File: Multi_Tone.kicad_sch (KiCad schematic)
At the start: 0 parts

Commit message: Added band-pass filter, ac-dc power, low-pass filter
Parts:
- added BR1: DB107-BP, symbol Device:D_Bridge_+-AA
- added C1, C3: 100u, symbol Device:C_Polarized
- added C2, C9: 470u, symbol Device:C_Polarized
- added C4, C5: 100n, symbol Device:C
- added C6: 10n, symbol Device:C
- added C7: 33n, symbol Device:C
- added D1: LED Y, symbol Device:LED
- added D2, D5: 1N4148, Diode_THT:D_DO-35_SOD27_P7.62mm_Horizontal, symbol Diode:1N4148
- added D3: LEDR, symbol Device:LED
- added D4: LEDG, symbol Device:LED
- added DR: R16, symbol Device:R
- added J1: PW_OUTPUT, symbol Connector_Generic:Conn_01x03
- added J2: PW_INPUT, symbol Connector_Generic:Conn_01x03
- added Q1, Q2: 2N3904, Package_TO_SOT_THT:TO-92_Inline, symbol Transistor_BJT:2N3904
- added R1: 1k, symbol Device:R
- added R10: 36k, symbol Device:R
- added R2, R6: 16K, symbol Device:R
- added R3, R4: 470R, symbol Device:R
- added R5, R7, R8: 4k7, symbol Device:R
- added R9: 47k, symbol Device:R
- added TP1, TP10, TP2, TP3, TP4, TP5, TP6, TP7, TP8, TP9: TestPoint, symbol Connector:TestPoint
- added U1: L7812, symbol Regulator_Linear:L7812
- added U2: L7912, symbol Regulator_Linear:L7912
- added U3, U4: LM2902, symbol Amplifier_Operational:LM2902
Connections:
- new net: D2.1 (K), R5.1
- new net: Q1.2 (B), R5.2, TP8.1
- new net: D3.2 (A), R4.2
- new net: BR1.1 (+), C9.1, U1.1 (IN)
- new net: BR1.2 (-), C2.2, U2.2 (VI)
- new net: C4.2, R2.2, R6.1
- new net: C6.1, C7.1, R10.1, R9.2
- new net: D5.1 (K), R7.1
- new net: Q2.2 (B), R7.2, TP9.1
- new net: D4.1 (K), Q2.3 (C)
- new net: D1.2 (A), R1.1
- new net: U3.13 (-), U3.14
- new net: D4.2 (A), R3.2
- new net: D3.1 (K), Q1.3 (C)
- new net: C7.2, R8.1, U3.6 (-)
- new net: C5.1, R6.2, U4.3 (+)
- new net +12V: C1.1, J1.3 (Pin_3), R3.1, R4.1, TP4.1, U1.3 (OUT)
- new net -12V: C3.2, D1.1 (K), J1.1 (Pin_1), TP5.1, U2.3 (VO)
- new net GND: C1.2, C3.1, C5.2, DR.2, J1.2 (Pin_2), Q1.1 (E), Q2.1 (E), R1.2, R9.1, TP3.1, TP6.1, U1.2 (GND), U2.1 (GND), U3.12 (+), U3.5 (+)
- new net GNDPWR: C2.1, C9.2, DR.1, J2.2 (Pin_2)
- new net OUT_LOW: C4.1, D2.2 (A), TP7.1, U4.1, U4.2 (-)
- new net OUT_MID: C6.2, D5.2 (A), R8.2, TP10.1, U3.7
- new net VAC+: BR1.3, J2.1 (Pin_1), TP1.1
- new net VAC-: BR1.4, J2.3 (Pin_3), TP2.1
- new net V_AMP: R10.2, R2.1
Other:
- note added: "AC TO DC +/-12V"
- note added: "LOW PASS FILTER"
- note added: "NEAR POWER INPUT"

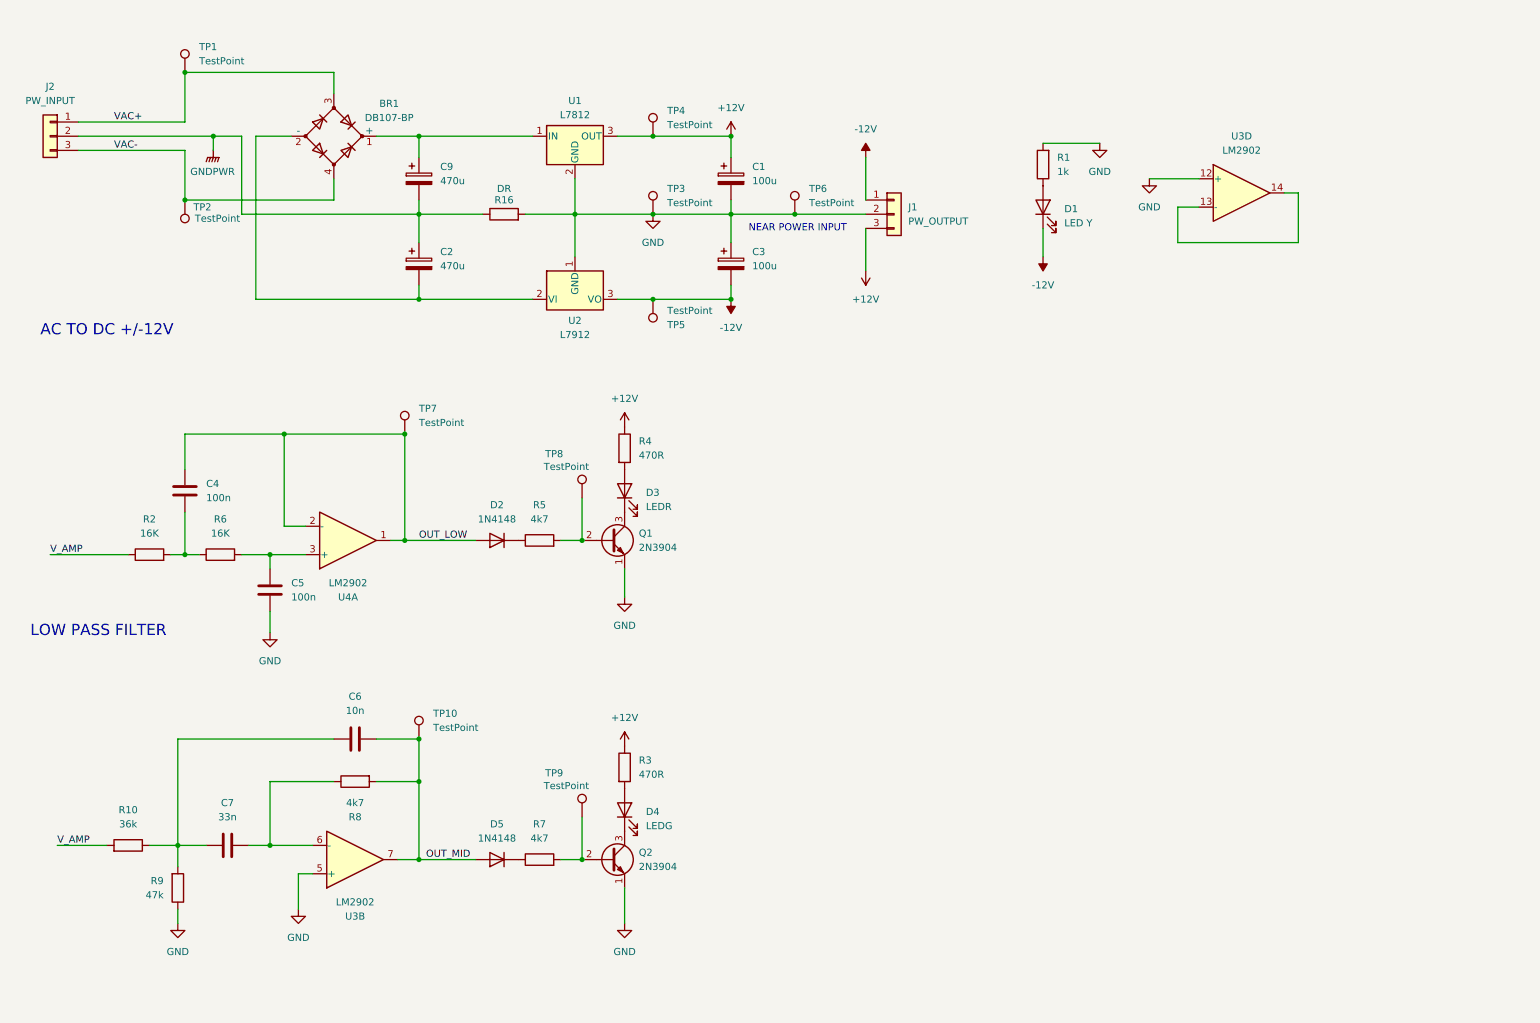
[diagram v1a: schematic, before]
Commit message: Completed schematic layout of music visualiser circuit.
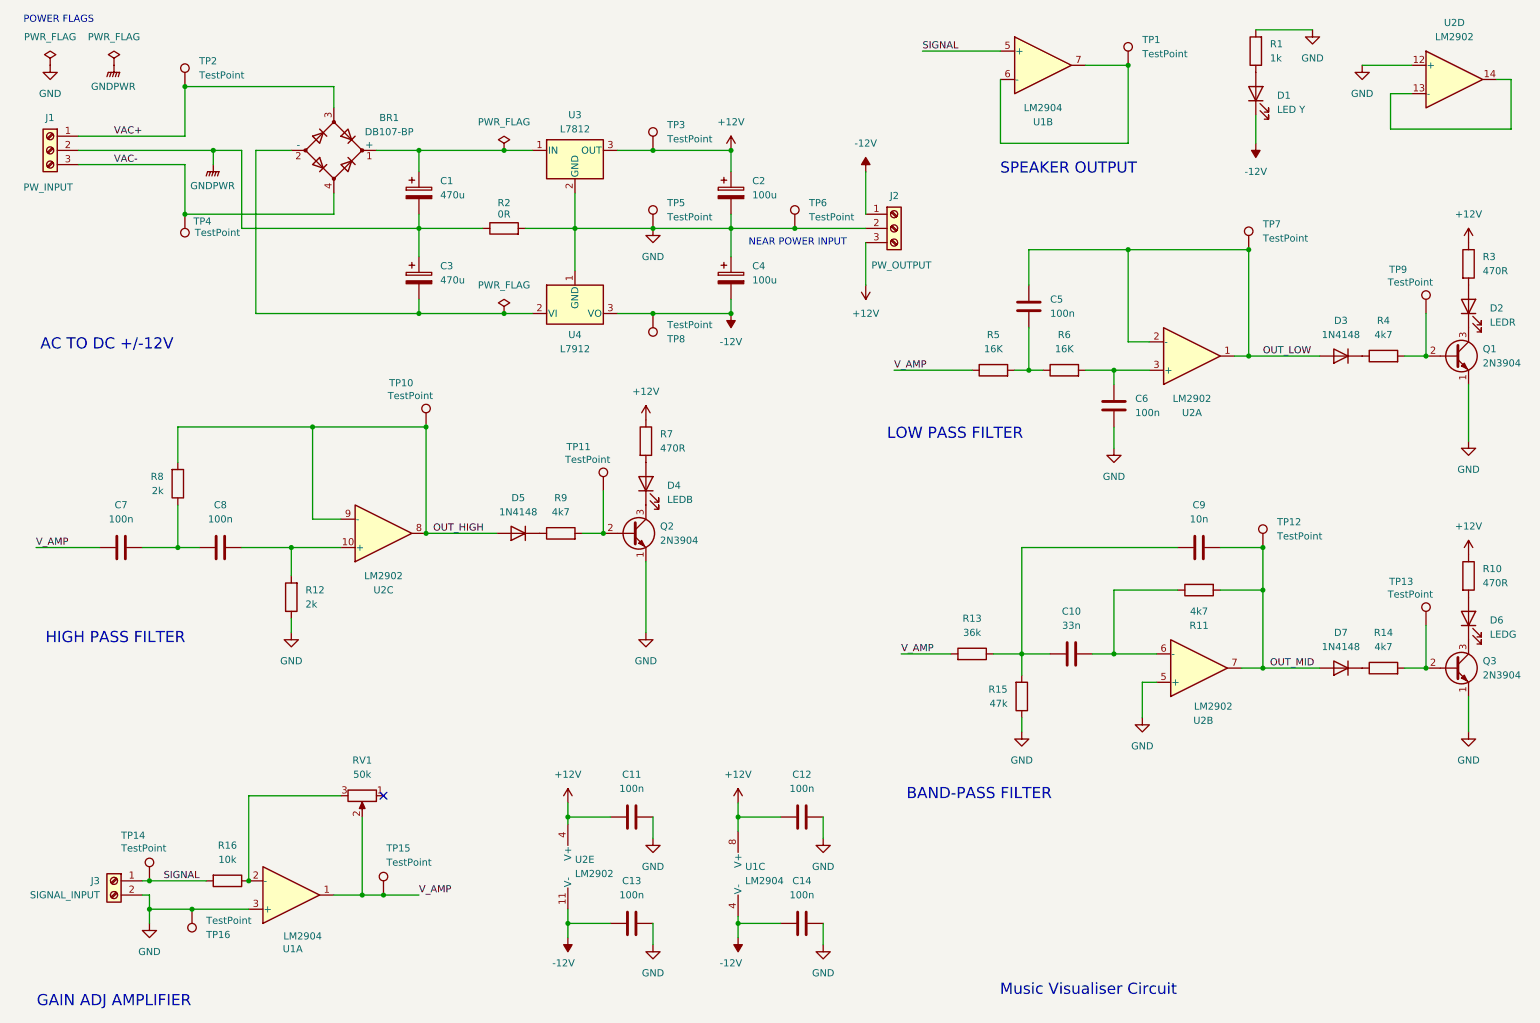
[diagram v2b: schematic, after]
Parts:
- removed J1: PW_OUTPUT, symbol Connector_Generic:Conn_01x03
- removed J2: PW_INPUT, symbol Connector_Generic:Conn_01x03
- added C11, C12, C13, C14, C7, C8: 100n, symbol Device:C
- added D4: LEDB, symbol Device:LED
- added D5: 1N4148, Diode_THT:D_DO-35_SOD27_P7.62mm_Horizontal, symbol Diode:1N4148
- added J1: PW_INPUT, symbol Connector:Screw_Terminal_01x03
- added J2: PW_OUTPUT, symbol Connector:Screw_Terminal_01x03
- added J3: SIGNAL_INPUT, symbol Connector:Screw_Terminal_01x02
- added Q2: 2N3904, Package_TO_SOT_THT:TO-92_Inline, symbol Transistor_BJT:2N3904
- added R12, R8: 2k, symbol Device:R
- added R16: 10k, symbol Device:R
- added R7: 470R, symbol Device:R
- added R9: 4k7, symbol Device:R
- added RV1: 50k, symbol Device:R_Potentiometer
- added TP1, TP10, TP11, TP14, TP15, TP16: TestPoint, symbol Connector:TestPoint
- added U1: LM2904, symbol Amplifier_Operational:LM2904
- added unit 5 of U2
- added unit 3 of U2
- R2: renamed from DR; value R16 -> 0R
- renumbered C9 to C1, C7 to C10, C1 to C2, C2 to C3, C3 to C4, C4 to C5, C5 to C6, C6 to C9, D3 to D2, D2 to D3, D4 to D6, D5 to D7, Q2 to Q3, R3 to R10, R8 to R11, R10 to R13, R7 to R14, R9 to R15, R4 to R3, R5 to R4, R2 to R5, TP10 to TP12, TP9 to TP13, TP1 to TP2, TP4 to TP3, TP2 to TP4, TP3 to TP5, TP5 to TP8, TP8 to TP9, U3 to U2, U4 to U2, U1 to U3, U2 to U4
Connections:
- net +12V: now also C11.1, C12.1, J2.3 (Pin_3), R7.1, U1.8 (V+), U2.4 (V+)
- net -12V: now also C13.2, C14.2, J2.1 (Pin_1), U1.4 (V-), U2.11 (V-)
- net GND: now also C11.2, C12.2, C13.1, C14.1, J2.2 (Pin_2), J3.2 (Pin_2), Q2.1 (E), R12.1, TP16.1, U1.3 (+)
- net GNDPWR: now also J1.2 (Pin_2)
- net VAC+: now also J1.1 (Pin_1)
- net VAC-: now also J1.3 (Pin_3)
- net V_AMP: now also C7.1, RV1.2, TP15.1, U1.1
- new net: C7.2, C8.1, R8.1
- new net: D5.1 (K), R9.1
- new net: C8.2, R12.2, U2.10 (+)
- new net: Q2.2 (B), R9.2, TP11.1
- new net: D4.1 (K), Q2.3 (C)
- new net: R16.1, RV1.3, U1.2 (-)
- new net: D4.2 (A), R7.2
- new net: TP1.1, U1.6 (-), U1.7
- new net OUT_HIGH: D5.2 (A), R8.2, TP10.1, U2.8, U2.9 (-)
- new net SIGNAL: J3.1 (Pin_1), R16.2, TP14.1, U1.5 (+)
- no-connect marks 0 -> 1
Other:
- note added: "BAND-PASS FILTER"
- note added: "GAIN ADJ AMPLIFIER"
- note added: "HIGH PASS FILTER"
- note added: "Music Visualiser Circuit"
- note added: "POWER FLAGS"
- note added: "SPEAKER OUTPUT"
- moved on the sheet: BR1, C1, C10, C2, C3, C4, C5, C6, C9, D1, D2, D3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

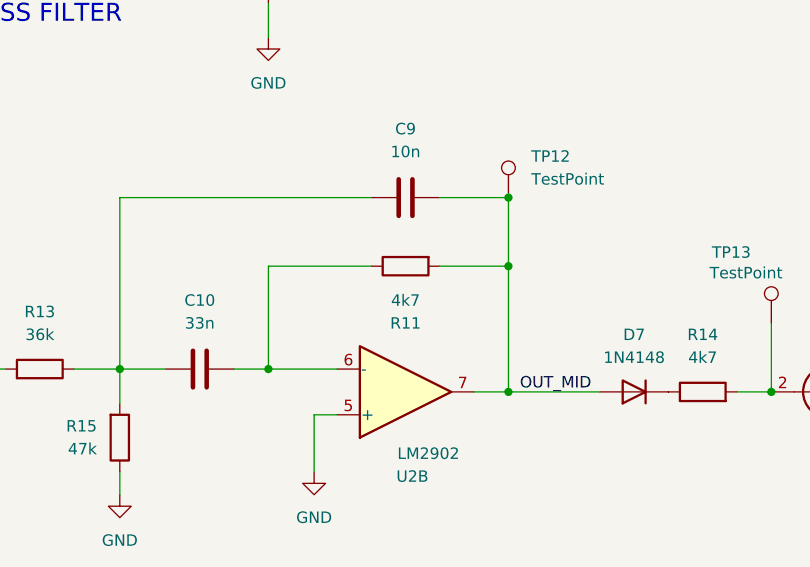
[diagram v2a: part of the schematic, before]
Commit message: Added footprints to schematic and changed band-pass filter resistor to 47k (R11)
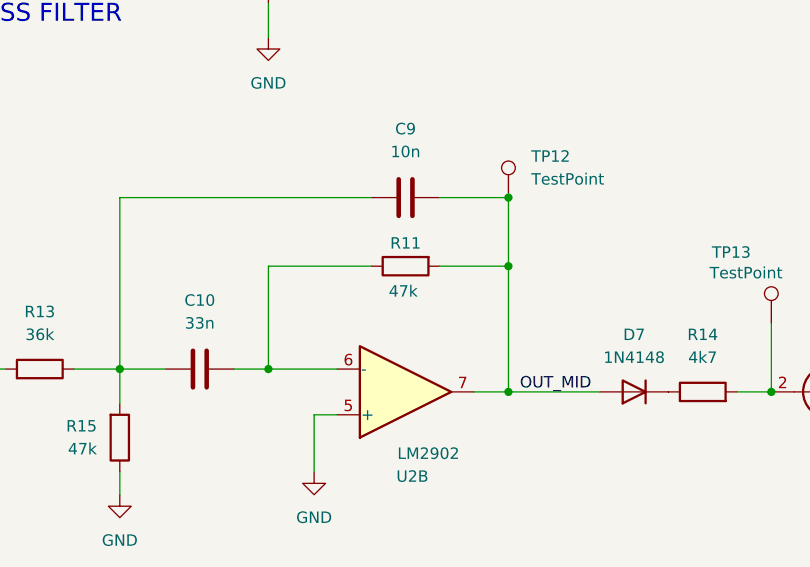
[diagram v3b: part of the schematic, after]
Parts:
- BR1: footprint (none) -> Diode_THT:Diode_Bridge_DIP-4_W7.62mm_P5.08mm
- C1, C2, C3, C4: footprint (none) -> Capacitor_THT:CP_Radial_D8.0mm_P3.50mm
- C10, C11, C12, C13, C14, C5, C6, C7, C8, C9: footprint (none) -> Capacitor_THT:C_Rect_L7.0mm_W2.5mm_P5.00mm
- D1, D2, D4, D6: footprint (none) -> LED_THT:LED_D3.0mm
- J1, J2: footprint (none) -> TerminalBlock_Phoenix:TerminalBlock_Phoenix_MKDS-1,5-3-5.08_1x03_P5.08mm_Horizontal
- J3: footprint (none) -> TerminalBlock_Phoenix:TerminalBlock_Phoenix_MKDS-1,5-2-5.08_1x02_P5.08mm_Horizontal
- R1, R12, R13, R15, R16, R5, R6, R8: footprint (none) -> Resistor_THT:R_Axial_DIN0207_L6.3mm_D2.5mm_P10.16mm_Horizontal
- R10, R14, R2, R3, R4, R7, R9: footprint (none) -> Resistor_SMD:R_2512_6332Metric
- R11: value 4k7 -> 47k; footprint (none) -> Resistor_THT:R_Axial_DIN0207_L6.3mm_D2.5mm_P10.16mm_Horizontal
- RV1: footprint (none) -> Potentiometer_THT:Potentiometer_Bourns_3299W_Vertical
- TP1, TP10, TP11, TP12, TP13, TP14, TP15, TP16, TP2, TP3, TP4, TP5, TP6, TP7, TP8, TP9: footprint (none) -> Connector_PinHeader_2.54mm:PinHeader_1x01_P2.54mm_Vertical
- U1: footprint (none) -> Package_DIP:DIP-8_W7.62mm
- U2: footprint (none) -> Package_DIP:DIP-14_W7.62mm
- U3, U4: footprint (none) -> Package_TO_SOT_THT:TO-220-3_Vertical
